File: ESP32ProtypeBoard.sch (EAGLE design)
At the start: 96 parts, among them IC1 SOIC-8, IC2 SI4431BDY, J10 POWER_JACKPTH_LOCK, Q2 MMBT3904, Q3 MMBT3904, U2 ESP-WROOM-32

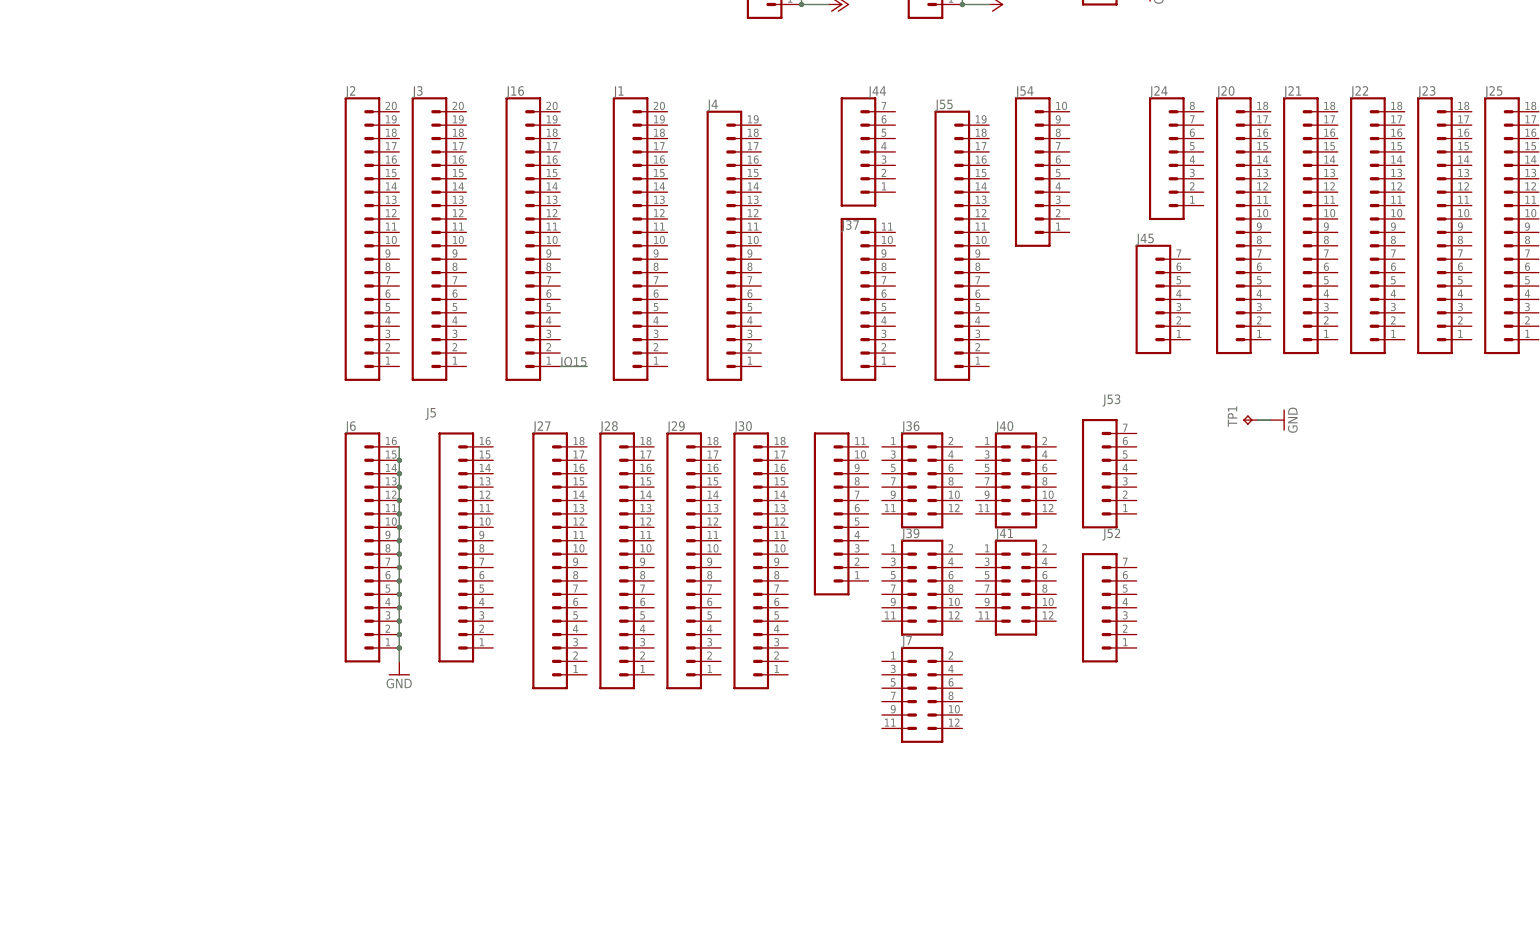
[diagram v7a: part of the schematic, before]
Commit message: Added connections for side empty pins
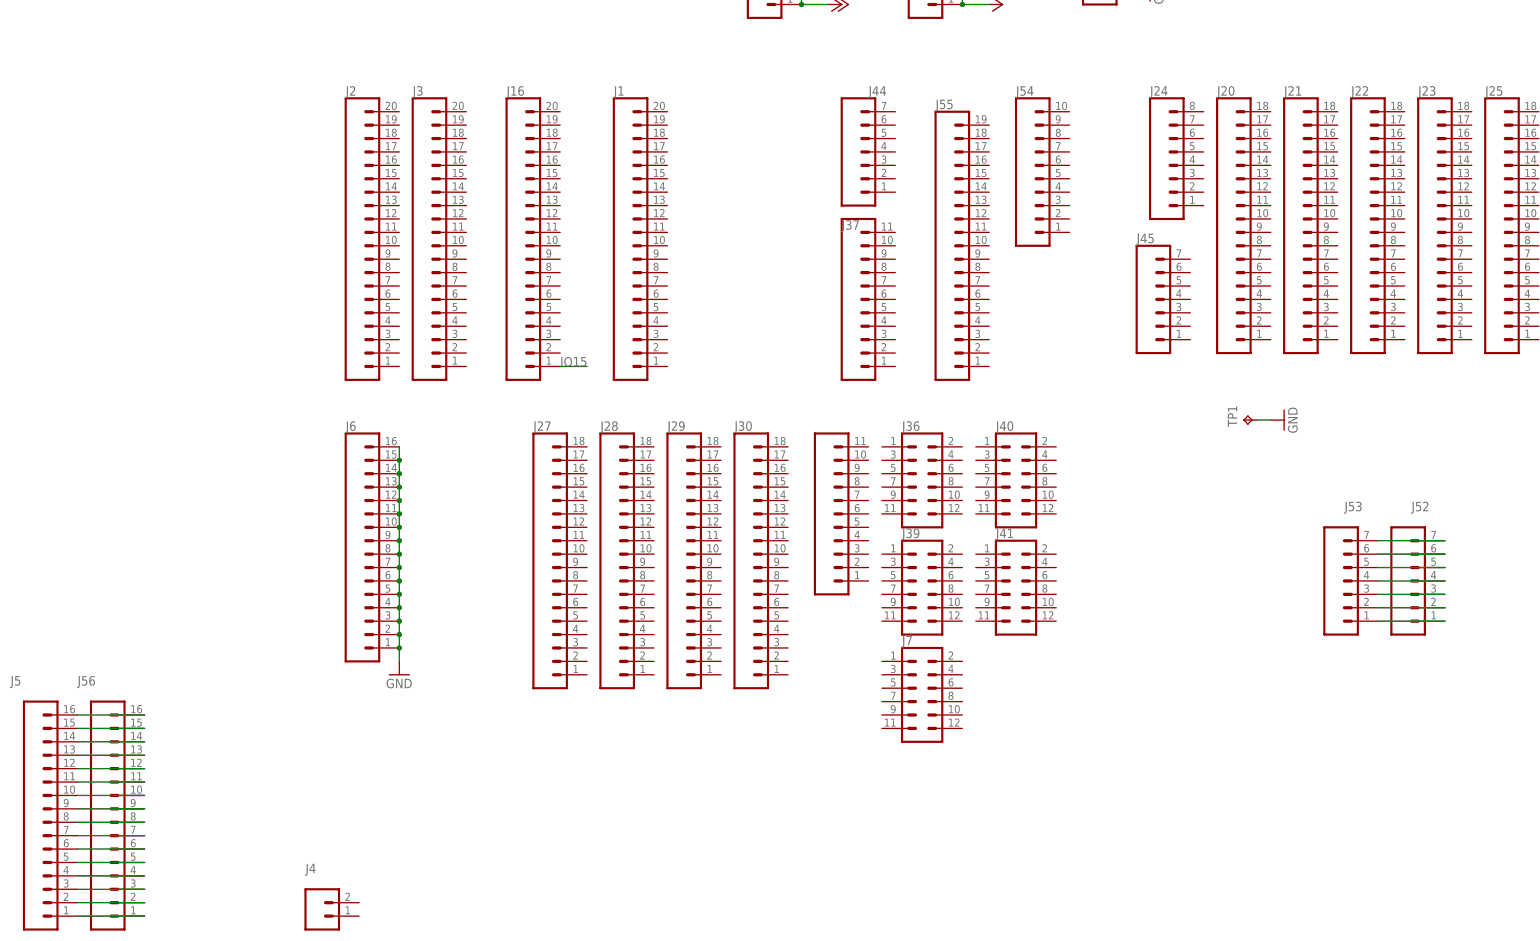
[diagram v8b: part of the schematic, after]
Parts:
- added J56: (no value), SparkFun-Connectors:CONN_161X16_NO_SILK
- J4: device SparkFun-Connectors:CONN_191X19_NO_SILK -> SparkFun-Connectors:CONN_021X02_NO_SILK
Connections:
- new net N$1: J5.16, J56.16
- new net N$11: J5.14, J56.14
- new net N$12: J5.13, J56.13
- new net N$2: J5.15, J56.15
- new net N$31: J5.12, J56.12
- new net N$32: J5.11, J56.11
- new net N$33: J5.10, J56.10
- new net N$34: J5.9, J56.9
- new net N$35: J5.8, J56.8
- new net N$36: J5.6, J56.6
- new net N$37: J5.7, J56.7
- new net N$38: J5.5, J56.5
- new net N$39: J5.4, J56.4
- new net N$40: J5.3, J56.3
- new net N$41: J5.2, J56.2
- new net N$42: J5.1, J56.1
- new net N$43: J52.7, J53.7
- new net N$44: J52.6, J53.6
- new net N$45: J52.5, J53.5
- new net N$46: J52.4, J53.4
- new net N$47: J52.3, J53.3
- new net N$48: J52.2, J53.2
- new net N$49: J52.1, J53.1
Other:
- moved on the sheet: J5, J52, J53
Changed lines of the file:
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@@
 <part name="D2" library="SparkFun-LED" deviceset="LED-GREEN" device="1206" value="BLUE"/>
 <part name="R1" library="eagle-ltspice" library_urn="urn:adsk.eagle:library:217" deviceset="R" device="R1206" package3d_urn="urn:adsk.eagle:package:13301/1" value="150R"/>
-<part name="J4" library="SparkFun-Connectors" deviceset="CONN_19" device="1X19_NO_SILK"/>
+<part name="J4" library="SparkFun-Connectors" library_urn="urn:adsk.eagle:library:513" deviceset="CONN_02" device="1X02_NO_SILK" package3d_urn="urn:adsk.eagle:package:38051/1"/>
 <part name="J5" library="SparkFun-Connectors" deviceset="CONN_16" device="1X16_NO_SILK"/>
 <part name="J6" library="SparkFun-Connectors" deviceset="CONN_16" device="1X16_NO_SILK"/>
@@
 <part name="C7" library="rcl" library_urn="urn:adsk.eagle:library:334" deviceset="C-EU" device="C1206" package3d_urn="urn:adsk.eagle:package:23618/2" value="(1uF)"/>
 <part name="J55" library="SparkFun-Connectors" library_urn="urn:adsk.eagle:library:513" deviceset="CONN_19" device="1X19_NO_SILK" package3d_urn="urn:adsk.eagle:package:38250/1"/>
+<part name="J56" library="SparkFun-Connectors" deviceset="CONN_16" device="1X16_NO_SILK"/>
 </parts>
 <sheets>
@@
 <attribute name="VALUE" x="298.958" y="77.47" size="1.778" layer="96" rot="R270"/>
 </instance>
-<instance part="J4" gate="G$1" x="96.52" y="-45.72" smashed="yes">
-<attribute name="VALUE" x="96.52" y="-73.406" size="1.778" layer="96" font="vector"/>
-<attribute name="NAME" x="96.52" y="-19.812" size="1.778" layer="95" font="vector"/>
-</instance>
-<instance part="J5" gate="G$1" x="45.72" y="-101.6" smashed="yes">
-<attribute name="VALUE" x="43.18" y="-129.286" size="1.778" layer="96" font="vector"/>
-<attribute name="NAME" x="43.18" y="-78.232" size="1.778" layer="95" font="vector"/>
+<instance part="J4" gate="G$1" x="22.86" y="-172.72" smashed="yes">
+<attribute name="VALUE" x="22.86" y="-200.406" size="1.778" layer="96" font="vector"/>
+<attribute name="NAME" x="20.32" y="-164.592" size="1.778" layer="95" font="vector"/>
+</instance>
+<instance part="J5" gate="G$1" x="-33.02" y="-152.4" smashed="yes">
+<attribute name="VALUE" x="-35.56" y="-180.086" size="1.778" layer="96" font="vector"/>
+<attribute name="NAME" x="-35.56" y="-129.032" size="1.778" layer="95" font="vector"/>
 </instance>
 <instance part="J6" gate="G$1" x="27.94" y="-101.6" smashed="yes">
@@
 <attribute name="NAME" x="403.86" y="30.988" size="1.778" layer="95" font="vector"/>
 </instance>
-<instance part="J52" gate="G$1" x="172.72" y="-116.84" smashed="yes">
-<attribute name="VALUE" x="171.45" y="-121.666" size="1.778" layer="96" font="vector"/>
-<attribute name="NAME" x="171.45" y="-101.092" size="1.778" layer="95" font="vector"/>
-</instance>
-<instance part="J53" gate="G$1" x="172.72" y="-91.44" smashed="yes">
-<attribute name="VALUE" x="171.45" y="-96.266" size="1.778" layer="96" font="vector"/>
-<attribute name="NAME" x="171.45" y="-75.692" size="1.778" layer="95" font="vector"/>
+<instance part="J52" gate="G$1" x="231.14" y="-111.76" smashed="yes">
+<attribute name="VALUE" x="229.87" y="-116.586" size="1.778" layer="96" font="vector"/>
+<attribute name="NAME" x="229.87" y="-96.012" size="1.778" layer="95" font="vector"/>
+</instance>
+<instance part="J53" gate="G$1" x="218.44" y="-111.76" smashed="yes">
+<attribute name="VALUE" x="217.17" y="-116.586" size="1.778" layer="96" font="vector"/>
+<attribute name="NAME" x="217.17" y="-96.012" size="1.778" layer="95" font="vector"/>
 </instance>
 <instance part="GND22" gate="1" x="38.1" y="-127" smashed="yes">
@@
 <attribute name="VALUE" x="139.7" y="-73.406" size="1.778" layer="96" font="vector"/>
 <attribute name="NAME" x="139.7" y="-19.812" size="1.778" layer="95" font="vector"/>
+</instance>
+<instance part="J56" gate="G$1" x="-20.32" y="-152.4" smashed="yes">
+<attribute name="VALUE" x="-22.86" y="-180.086" size="1.778" layer="96" font="vector"/>
+<attribute name="NAME" x="-22.86" y="-129.032" size="1.778" layer="95" font="vector"/>
 </instance>
 </instances>
@@
 </segment>
 </net>
+<net name="N$1" class="0">
+<segment>
+<pinref part="J5" gate="G$1" pin="16"/>
+<pinref part="J56" gate="G$1" pin="16"/>
+<wire x1="-22.86" y1="-134.62" x2="-10.16" y2="-134.62" width="0.1524" layer="91"/>
+</segment>
+</net>
+<net name="N$2" class="0">
+<segment>
+<pinref part="J56" gate="G$1" pin="15"/>
+<pinref part="J5" gate="G$1" pin="15"/>
+<wire x1="-10.16" y1="-137.16" x2="-22.86" y2="-137.16" width="0.1524" layer="91"/>
+</segment>
+</net>
+<net name="N$11" class="0">
+<segment>
+<pinref part="J5" gate="G$1" pin="14"/>
+<pinref part="J56" gate="G$1" pin="14"/>
+<wire x1="-22.86" y1="-139.7" x2="-10.16" y2="-139.7" width="0.1524" layer="91"/>
+</segment>
+</net>
+<net name="N$12" class="0">
+<segment>
+<pinref part="J56" gate="G$1" pin="13"/>
+<pinref part="J5" gate="G$1" pin="13"/>
+<wire x1="-10.16" y1="-142.24" x2="-22.86" y2="-142.24" width="0.1524" layer="91"/>
+</segment>
+</net>
+<net name="N$31" class="0">
+<segment>
+<pinref part="J5" gate="G$1" pin="12"/>
+<pinref part="J56" gate="G$1" pin="12"/>
+<wire x1="-22.86" y1="-144.78" x2="-10.16" y2="-144.78" width="0.1524" layer="91"/>
+</segment>
+</net>
+<net name="N$32" class="0">
+<segment>
+<pinref part="J56" gate="G$1" pin="11"/>
+<pinref part="J5" gate="G$1" pin="11"/>
+<wire x1="-10.16" y1="-147.32" x2="-22.86" y2="-147.32" width="0.1524" layer="91"/>
+</segment>
+</net>
+<net name="N$33" class="0">
+<segment>
+<pinref part="J5" gate="G$1" pin="10"/>
+<pinref part="J56" gate="G$1" pin="10"/>
+<wire x1="-22.86" y1="-149.86" x2="-10.16" y2="-149.86" width="0.1524" layer="91"/>
+</segment>
+</net>
+<net name="N$34" class="0">
+<segment>
+<pinref part="J56" gate="G$1" pin="9"/>
+<pinref part="J5" gate="G$1" pin="9"/>
+<wire x1="-10.16" y1="-152.4" x2="-22.86" y2="-152.4" width="0.1524" layer="91"/>
+</segment>
+</net>
+<net name="N$35" class="0">
+<segment>
+<pinref part="J5" gate="G$1" pin="8"/>
+<pinref part="J56" gate="G$1" pin="8"/>
+<wire x1="-22.86" y1="-154.94" x2="-10.16" y2="-154.94" width="0.1524" layer="91"/>
+</segment>
+</net>
+<net name="N$36" class="0">
+<segment>
+<pinref part="J56" gate="G$1" pin="6"/>
+<pinref part="J5" gate="G$1" pin="6"/>
+<wire x1="-10.16" y1="-160.02" x2="-22.86" y2="-160.02" width="0.1524" layer="91"/>
+</segment>
+</net>
+<net name="N$37" class="0">
+<segment>
+<pinref part="J5" gate="G$1" pin="7"/>
+<pinref part="J56" gate="G$1" pin="7"/>
+<wire x1="-22.86" y1="-157.48" x2="-10.16" y2="-157.48" width="0.1524" layer="91"/>
+</segment>
+</net>
+<net name="N$38" class="0">
+<segment>
+<pinref part="J56" gate="G$1" pin="5"/>
+<pinref part="J5" gate="G$1" pin="5"/>
+<wire x1="-10.16" y1="-162.56" x2="-22.86" y2="-162.56" width="0.1524" layer="91"/>
+</segment>
+</net>
+<net name="N$39" class="0">
+<segment>
+<pinref part="J5" gate="G$1" pin="4"/>
+<pinref part="J56" gate="G$1" pin="4"/>
+<wire x1="-22.86" y1="-165.1" x2="-10.16" y2="-165.1" width="0.1524" layer="91"/>
+</segment>
+</net>
+<net name="N$40" class="0">
+<segment>
+<pinref part="J56" gate="G$1" pin="3"/>
+<pinref part="J5" gate="G$1" pin="3"/>
+<wire x1="-10.16" y1="-167.64" x2="-22.86" y2="-167.64" width="0.1524" layer="91"/>
+</segment>
+</net>
+<net name="N$41" class="0">
+<segment>
+<pinref part="J5" gate="G$1" pin="2"/>
+<pinref part="J56" gate="G$1" pin="2"/>
+<wire x1="-22.86" y1="-170.18" x2="-10.16" y2="-170.18" width="0.1524" layer="91"/>
+</segment>
+</net>
+<net name="N$42" class="0">
+<segment>
+<pinref part="J56" gate="G$1" pin="1"/>
+<pinref part="J5" gate="G$1" pin="1"/>
+<wire x1="-10.16" y1="-172.72" x2="-22.86" y2="-172.72" width="0.1524" layer="91"/>
+</segment>
+</net>
+<net name="N$43" class="0">
+<segment>
+<pinref part="J53" gate="G$1" pin="7"/>
+<pinref part="J52" gate="G$1" pin="7"/>
+<wire x1="223.52" y1="-101.6" x2="236.22" y2="-101.6" width="0.1524" layer="91"/>
+</segment>
+</net>
+<net name="N$44" class="0">
+<segment>
+<pinref part="J52" gate="G$1" pin="6"/>
+<pinref part="J53" gate="G$1" pin="6"/>
+<wire x1="236.22" y1="-104.14" x2="223.52" y2="-104.14" width="0.1524" layer="91"/>
+</segment>
+</net>
+<net name="N$45" class="0">
+<segment>
+<pinref part="J53" gate="G$1" pin="5"/>
+<pinref part="J52" gate="G$1" pin="5"/>
+<wire x1="223.52" y1="-106.68" x2="236.22" y2="-106.68" width="0.1524" layer="91"/>
+</segment>
+</net>
+<net name="N$46" class="0">
+<segment>
+<pinref part="J52" gate="G$1" pin="4"/>
+<pinref part="J53" gate="G$1" pin="4"/>
+<wire x1="236.22" y1="-109.22" x2="223.52" y2="-109.22" width="0.1524" layer="91"/>
+</segment>
+</net>
+<net name="N$47" class="0">
+<segment>
+<pinref part="J53" gate="G$1" pin="3"/>
+<pinref part="J52" gate="G$1" pin="3"/>
+<wire x1="223.52" y1="-111.76" x2="236.22" y2="-111.76" width="0.1524" layer="91"/>
+</segment>
+</net>
+<net name="N$48" class="0">
+<segment>
+<pinref part="J53" gate="G$1" pin="2"/>
+<pinref part="J52" gate="G$1" pin="2"/>
+<wire x1="223.52" y1="-114.3" x2="236.22" y2="-114.3" width="0.1524" layer="91"/>
+</segment>
+</net>
+<net name="N$49" class="0">
+<segment>
+<pinref part="J52" gate="G$1" pin="1"/>
+<pinref part="J53" gate="G$1" pin="1"/>
+<wire x1="236.22" y1="-116.84" x2="223.52" y2="-116.84" width="0.1524" layer="91"/>
+</segment>
+</net>
